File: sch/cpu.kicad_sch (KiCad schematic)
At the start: 12 parts

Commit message: Sch: CPU - part annotations
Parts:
- D5: value (none) -> 74LS74
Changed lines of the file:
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@@
     (in_bom yes) (on_board yes)
     (property "Reference" "R10" (id 0) (at 38.735 102.235 90))
-    (property "Value" "" (id 1) (at 45.72 102.235 90))
+    (property "Value" "" (id 1) (at 43.18 102.235 90))
     (property "Footprint" "" (id 2) (at 40.005 99.695 0)
       (effects (font (size 1.27 1.27)) hide)
@@
       (effects (font (size 1.27 1.27)) (justify left))
     )
-    (property "Value" "" (id 1) (at 61.595 72.39 0)
+    (property "Value" "74LS74" (id 1) (at 61.595 72.39 0)
       (effects (font (size 1.27 1.27)) (justify left))
     )
@@
       (effects (font (size 1.27 1.27)) hide)
     )
-    (property "Value" "" (id 1) (at 34.29 99.6949 90)
-      (effects (font (size 1.27 1.27)) (justify left))
-    )
+    (property "Value" "+5V" (id 1) (at 34.29 99.6949 90)
+      (effects (font (size 1.27 1.27)) (justify left))
+    )

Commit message: Sch: CPU - add R10 value
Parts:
- R10: value (none) -> 1k
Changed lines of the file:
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@@
     (in_bom yes) (on_board yes)
     (property "Reference" "R10" (id 0) (at 38.735 102.235 90))
-    (property "Value" "" (id 1) (at 43.18 102.235 90))
+    (property "Value" "1k" (id 1) (at 43.18 102.235 90))
     (property "Footprint" "" (id 2) (at 40.005 99.695 0)
       (effects (font (size 1.27 1.27)) hide)

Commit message: Schematics completed with values
Visual corrections pending
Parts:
- D5: value 74LS74 -> 7474
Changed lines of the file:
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@@
       (effects (font (size 1.27 1.27)) (justify left))
     )
-    (property "Value" "74LS74" (id 1) (at 61.595 72.39 0)
+    (property "Value" "7474" (id 1) (at 61.595 72.39 0)
       (effects (font (size 1.27 1.27)) (justify left))
     )

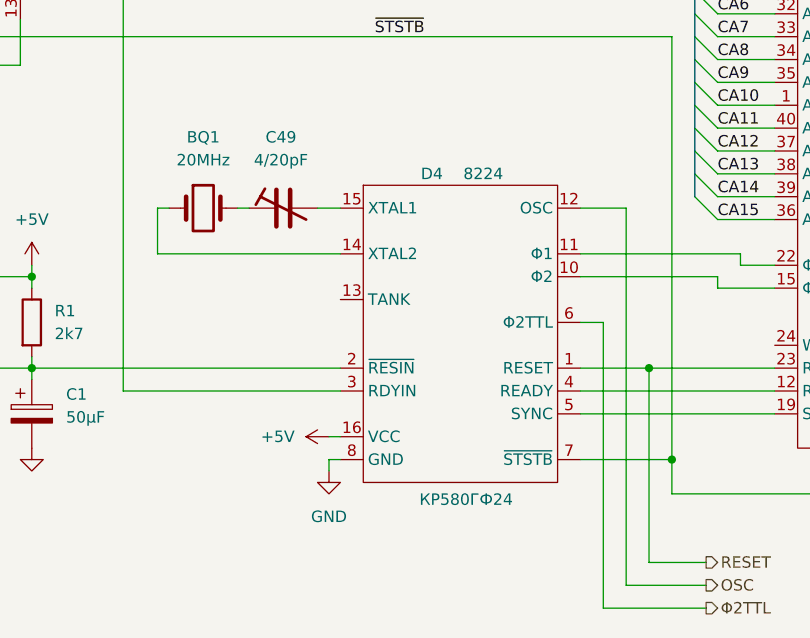
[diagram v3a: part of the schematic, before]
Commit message: Sch: fixed 8224 symbol (missing +12V power pin)
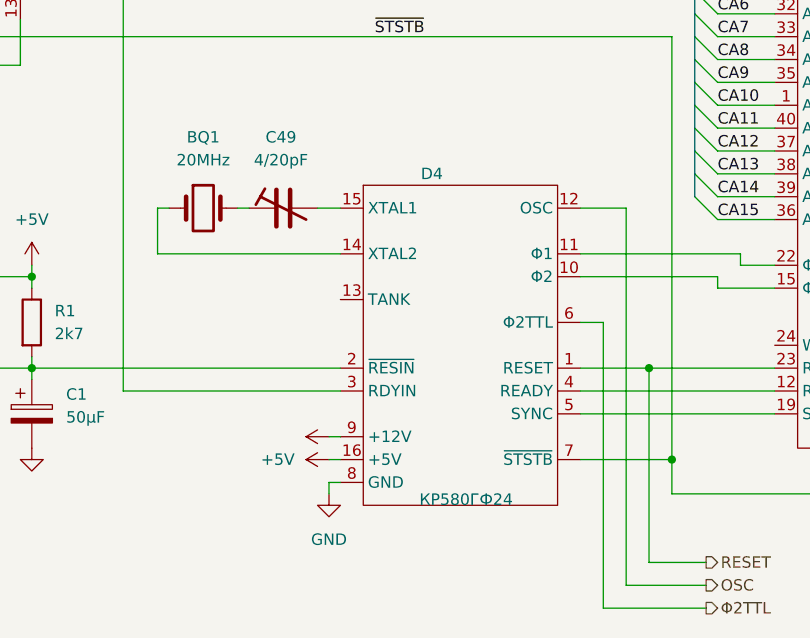
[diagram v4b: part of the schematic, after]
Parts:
- D4: value 8224 -> (none)
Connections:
- net +12V: now also D4.9 (+12V)
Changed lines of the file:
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@@
     (stroke (width 0) (type default) (color 0 0 0 0))
   )
-  (wire (pts (xy 82.55 144.78) (xy 82.55 143.51))
+  (wire (pts (xy 82.55 147.32) (xy 82.55 146.05))
     (stroke (width 0) (type default) (color 0 0 0 0))
   )
@@
     (stroke (width 0) (type default) (color 0 0 0 0))
   )
+  (wire (pts (xy 82.55 143.51) (xy 83.82 143.51))
+    (stroke (width 0) (type default) (color 0 0 0 0))
+  )
+  (wire (pts (xy 39.37 86.995) (xy 40.64 86.995))
+    (stroke (width 0) (type default) (color 0 0 0 0))
+  )
+  (wire (pts (xy 171.45 45.72) (xy 179.07 45.72))
+    (stroke (width 0) (type default) (color 0 0 0 0))
+  )
+  (bus (pts (xy 168.91 30.48) (xy 168.91 33.02))
+    (stroke (width 0) (type default) (color 0 0 0 0))
+  )
+  (wire (pts (xy 125.73 83.82) (xy 132.08 83.82))
+    (stroke (width 0) (type default) (color 0 0 0 0))
+  )
+  (bus (pts (xy 123.19 62.23) (xy 123.19 76.2))
+    (stroke (width 0) (type default) (color 0 0 0 0))
+  )
+  (bus (pts (xy 213.36 78.74) (xy 213.36 76.2))
+    (stroke (width 0) (type default) (color 0 0 0 0))
+  )
+  (wire (pts (xy 125.73 78.74) (xy 132.08 78.74))
+    (stroke (width 0) (type default) (color 0 0 0 0))
+  )
+  (bus (pts (xy 123.19 62.23) (xy 168.91 62.23))
+    (stroke (width 0) (type default) (color 0 0 0 0))
+  )
+  (wire (pts (xy 204.47 91.44) (xy 210.82 91.44))
+    (stroke (width 0) (type default) (color 0 0 0 0))
+  )
+  (wire (pts (xy 128.27 121.92) (xy 132.08 121.92))
+    (stroke (width 0) (type default) (color 0 0 0 0))
+  )
+  (wire (pts (xy 125.73 99.06) (xy 132.08 99.06))
+    (stroke (width 0) (type default) (color 0 0 0 0))
+  )
   (wire (pts (xy 82.55 140.97) (xy 83.82 140.97))
     (stroke (width 0) (type default) (color 0 0 0 0))
   )
-  (wire (pts (xy 39.37 86.995) (xy 40.64 86.995))
-    (stroke (width 0) (type default) (color 0 0 0 0))
-  )
-  (wire (pts (xy 171.45 45.72) (xy 179.07 45.72))
-    (stroke (width 0) (type default) (color 0 0 0 0))
-  )
-  (bus (pts (xy 168.91 30.48) (xy 168.91 33.02))
-    (stroke (width 0) (type default) (color 0 0 0 0))
-  )
-  (wire (pts (xy 125.73 83.82) (xy 132.08 83.82))
-    (stroke (width 0) (type default) (color 0 0 0 0))
-  )
-  (bus (pts (xy 123.19 62.23) (xy 123.19 76.2))
-    (stroke (width 0) (type default) (color 0 0 0 0))
-  )
-  (bus (pts (xy 213.36 78.74) (xy 213.36 76.2))
-    (stroke (width 0) (type default) (color 0 0 0 0))
-  )
-  (wire (pts (xy 125.73 78.74) (xy 132.08 78.74))
-    (stroke (width 0) (type default) (color 0 0 0 0))
-  )
-  (bus (pts (xy 123.19 62.23) (xy 168.91 62.23))
-    (stroke (width 0) (type default) (color 0 0 0 0))
-  )
-  (wire (pts (xy 204.47 91.44) (xy 210.82 91.44))
-    (stroke (width 0) (type default) (color 0 0 0 0))
-  )
-  (wire (pts (xy 128.27 121.92) (xy 132.08 121.92))
-    (stroke (width 0) (type default) (color 0 0 0 0))
-  )
-  (wire (pts (xy 125.73 99.06) (xy 132.08 99.06))
-    (stroke (width 0) (type default) (color 0 0 0 0))
-  )
   (wire (pts (xy 171.45 33.02) (xy 179.07 33.02))
     (stroke (width 0) (type default) (color 0 0 0 0))
@@
     (stroke (width 0) (type default) (color 0 0 0 0))
   )
-  (wire (pts (xy 82.55 143.51) (xy 83.82 143.51))
+  (wire (pts (xy 82.55 146.05) (xy 83.82 146.05))
     (stroke (width 0) (type default) (color 0 0 0 0))
   )
@@
     (pin "1")
   )
-  (symbol (lib_id "power:GND") (at 82.55 144.78 0) (unit 1)
-    (in_bom yes) (on_board yes) (fields_autoplaced)
-    (property "Reference" "#PWR?" (id 0) (at 82.55 151.13 0)
-      (effects (font (size 1.27 1.27)) hide)
-    )
-    (property "Value" "GND" (id 1) (at 82.55 149.86 0))
-    (property "Footprint" "" (id 2) (at 82.55 144.78 0)
-      (effects (font (size 1.27 1.27)) hide)
-    )
-    (property "Datasheet" "" (id 3) (at 82.55 144.78 0)
+  (symbol (lib_id "power:GND") (at 82.55 147.32 0) (unit 1)
+    (in_bom yes) (on_board yes) (fields_autoplaced)
+    (property "Reference" "#PWR?" (id 0) (at 82.55 153.67 0)
+      (effects (font (size 1.27 1.27)) hide)
+    )
+    (property "Value" "GND" (id 1) (at 82.55 152.4 0))
+    (property "Footprint" "" (id 2) (at 82.55 147.32 0)
+      (effects (font (size 1.27 1.27)) hide)
+    )
+    (property "Datasheet" "" (id 3) (at 82.55 147.32 0)
       (effects (font (size 1.27 1.27)) hide)
     )
@@
     (pin "2")
   )
+  (symbol (lib_id "power:+12V") (at 82.55 140.97 90) (unit 1)
+    (in_bom yes) (on_board yes) (fields_autoplaced)
+    (property "Reference" "#PWR?" (id 0) (at 86.36 140.97 0)
+      (effects (font (size 1.27 1.27)) hide)
+    )
+    (property "Value" "" (id 1) (at 78.74 140.9699 90)
+      (effects (font (size 1.27 1.27)) (justify left))
+    )
+    (property "Footprint" "" (id 2) (at 82.55 140.97 0)
+      (effects (font (size 1.27 1.27)) hide)
+    )
+    (property "Datasheet" "" (id 3) (at 82.55 140.97 0)
+      (effects (font (size 1.27 1.27)) hide)
+    )
+    (pin "1")
+  )
   (symbol (lib_id "power:+5V") (at 149.86 50.8 270) (unit 1)
     (in_bom yes) (on_board yes) (fields_autoplaced)
@@
     (in_bom yes) (on_board yes)
     (property "Reference" "D4" (id 0) (at 93.98 111.76 0))
-    (property "Value" "8224" (id 1) (at 99.695 111.76 0))
+    (property "Value" "" (id 1) (at 99.695 111.76 0))
     (property "Footprint" "" (id 2) (at 86.36 113.03 0)
       (effects (font (size 1.27 1.27)) hide)
@@
     (pin "7")
     (pin "8")
+    (pin "9")
   )
   (symbol (lib_id "intel8080:8228") (at 185.42 76.2 0) (unit 1)
@@
     (pin "9")
   )
-  (symbol (lib_id "power:+5V") (at 82.55 140.97 90) (unit 1)
-    (in_bom yes) (on_board yes) (fields_autoplaced)
-    (property "Reference" "#PWR?" (id 0) (at 86.36 140.97 0)
-      (effects (font (size 1.27 1.27)) hide)
-    )
-    (property "Value" "+5V" (id 1) (at 78.74 140.9699 90)
-      (effects (font (size 1.27 1.27)) (justify left))
-    )
-    (property "Footprint" "" (id 2) (at 82.55 140.97 0)
-      (effects (font (size 1.27 1.27)) hide)
-    )
-    (property "Datasheet" "" (id 3) (at 82.55 140.97 0)
-      (effects (font (size 1.27 1.27)) hide)
-    )
+  (symbol (lib_id "power:+5V") (at 82.55 143.51 90) (unit 1)
+    (in_bom yes) (on_board yes) (fields_autoplaced)
+    (property "Reference" "#PWR?" (id 0) (at 86.36 143.51 0)
+      (effects (font (size 1.27 1.27)) hide)
+    )
+    (property "Value" "+5V" (id 1) (at 78.74 143.5099 90)
+      (effects (font (size 1.27 1.27)) (justify left))
+    )
+    (property "Footprint" "" (id 2) (at 82.55 143.51 0)
+      (effects (font (size 1.27 1.27)) hide)
+    )
+    (property "Datasheet" "" (id 3) (at 82.55 143.51 0)
+      (effects (font (size 1.27 1.27)) hide)
+    )
